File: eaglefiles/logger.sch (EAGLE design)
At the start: 15 parts, among them IC2 MAX641CSA

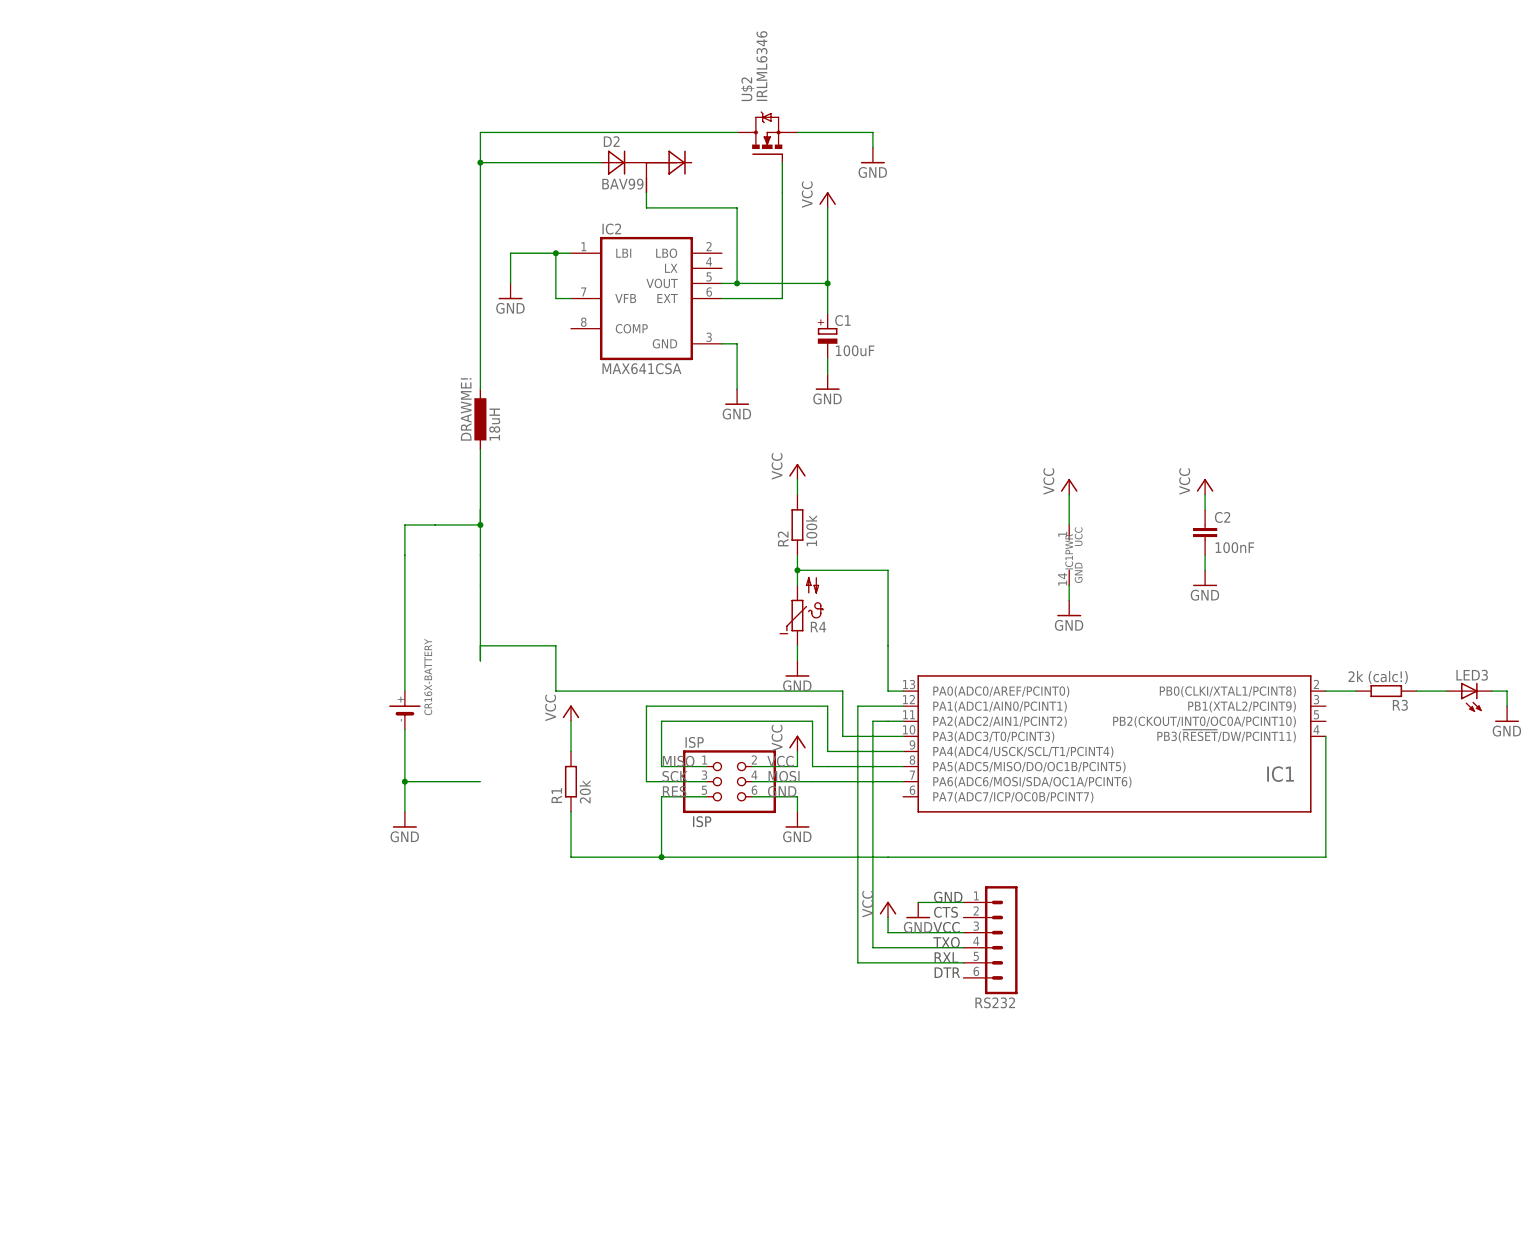
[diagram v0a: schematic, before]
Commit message: UART-USB Adapter and TSIC-506 added
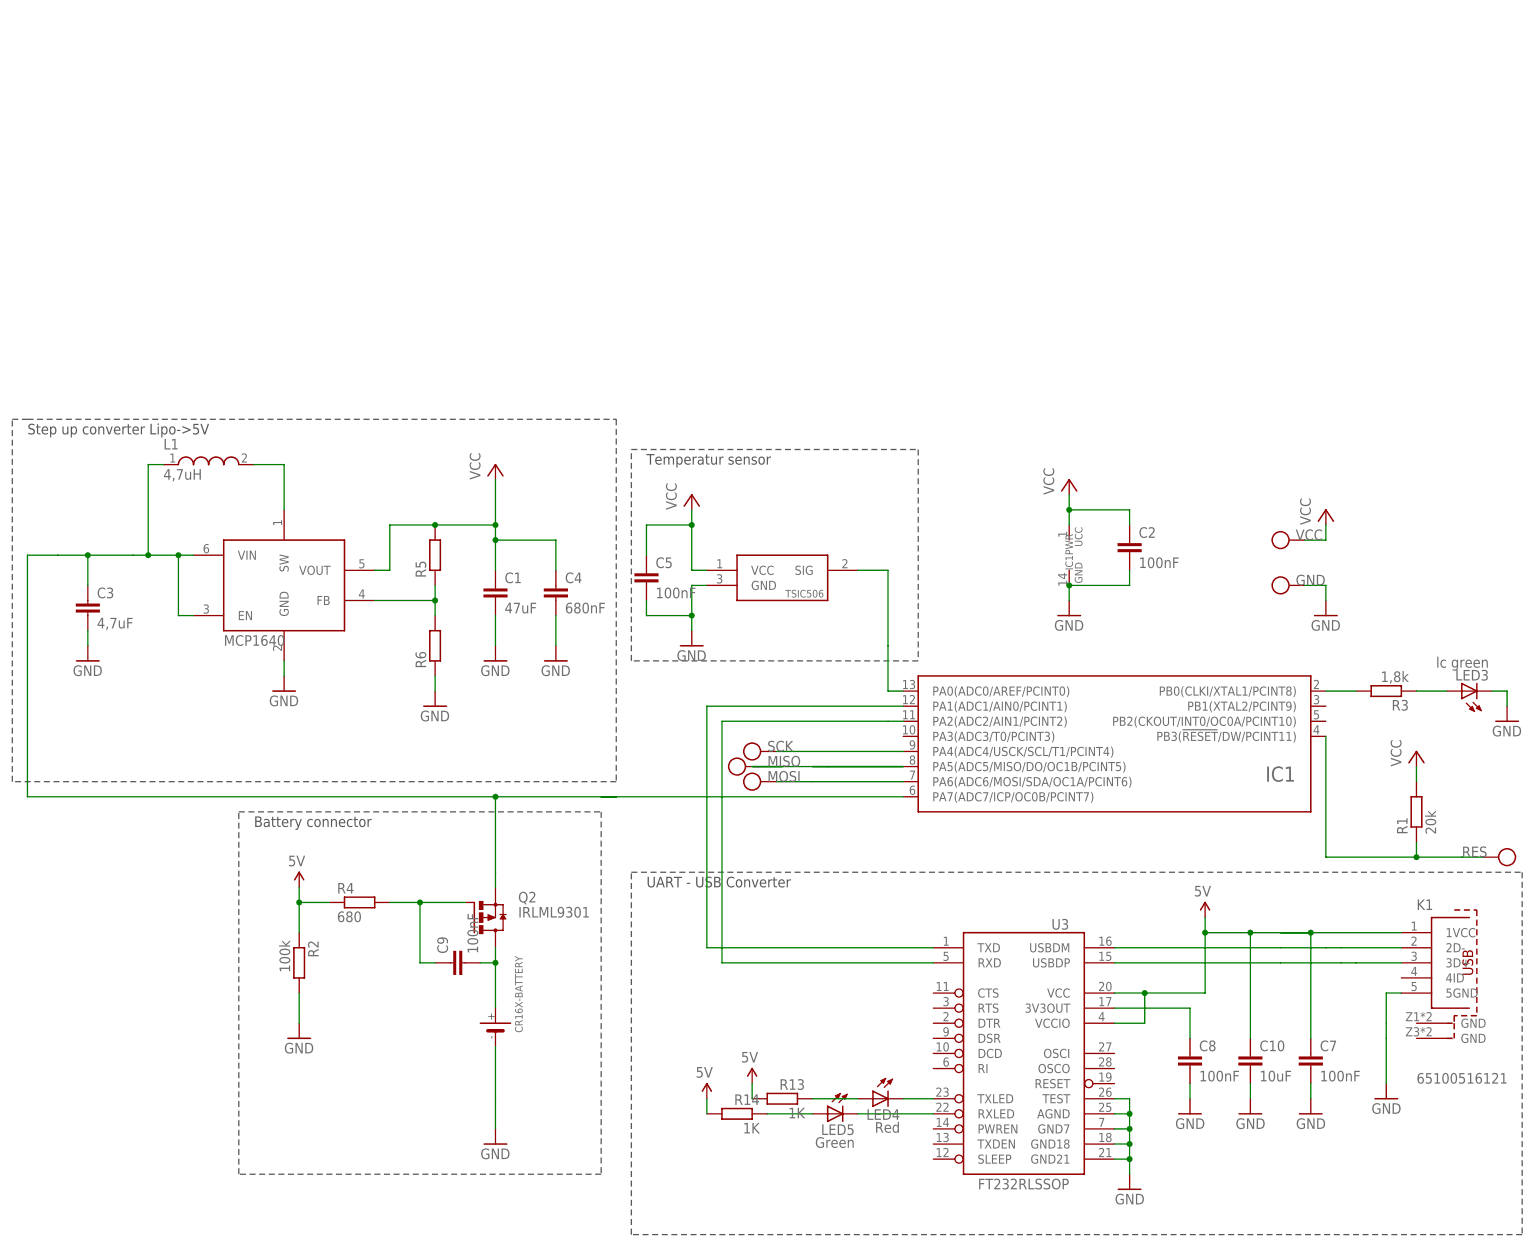
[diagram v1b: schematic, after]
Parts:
- removed D2: BAV99, 0liver:BAV99
- removed DRAWME!: 18uH, rcl:L-EUL8530M
- removed IC2: MAX641CSA, maxim:MAX641CSA
- removed ISP: (no value), pinhead:PINHD-2X3
- removed RS232: (no value), con-lstb:MA06-1
- added C10: 10uF, rcl:C-EUC1206
- added C3: 4,7uF, rcl:C-EUC1206K
- added C4: 680nF, resistor:C-EUC0805
- added C5, C8, C9: 100nF, rcl:C-EUC0603
- added C7: 100nF, rcl:C-EUC1206
- added K1: 65100516121, Input-Output_Connectors_rev15d:65100516121
- added L1: 4,7uH, EagleLibrary_Wuerth_Elektronik_eiSos_rev16a:WE-TPC_3816
- added LED4: Red, SparkFun:LED0603
- added LED5: Green, SparkFun:LED0603
- added Q2: IRLML9301, 0liver:IRLML9301
- added R13, R14: 1K, rcl:R-EU_R1206
- added R5, R6: (no value), resistor:R-EU_R1206
- added U$10, U$11, U$12, U$7, U$8, U$9: (no value), 0liver:PIN1.27
- added U1: MCP1640, karlnet-parts:MCP1640
- added U3: FT232RLSSOP, SparkFun:FT232RLSSOP
- C1: value 100uF -> 47uF; device rcl:CPOL-EU153CLV-0505 -> resistor:C-EUC1206
- LED3: value (none) -> lc green; device led:LEDSML0603 -> led:LEDCHIPLED_0603
- R2: device rcl:R-EU_R1206 -> eagle-ltspice:RR1206
- R3: value 2k (calc!) -> 1,8k
- R4: value (none) -> 680; device ptc-ntc:NTC640 -> eagle-ltspice:RR1206
- U$2: value IRLML6346 -> TSIC-506; device 0liver:IRLML6346 -> 0liver:TSIC-506
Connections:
- removed net D1: IC1IC.PA3(ADC3/T0/PCINT3), U$1.P$1
- removed net N$8: D2.A, DRAWME!.1, U$2.D
- new net 5V: R2.1, R4.1
- new net N$3: C8.1, U3.3V3OUT
- new net N$4: LED4.A, R13.1
- new net N$6: C9.2, Q2.D, U$1.P$1
- new net RXLED: LED5.C, U3.RXLED
- new net SW: L1.2, U1.SW
- new net TXLED: LED4.C, U3.TXLED
- new net USB_D+: K1.3D+, U3.USBDP
- new net USB_D-: K1.2D-, U3.USBDM
- new net VSUPPLY: C3.1, IC1IC.PA7(ADC7/ICP/OC0B/PCINT7), L1.1, Q2.S, U1.EN, U1.VIN
- new net V_USB: C10.1, C7.1, C9.1, K1.1VCC, Q2.G, R13.2, R14.2, R4.2, U3.VCC, U3.VCCIO
- net GND: now also C1.2, C10.2, C3.2, C4.2, C5.2, C7.2, C8.2, K1.5GND, R2.2, R6.1, U$10.P$1, U$2.GND, U1.GND, U3.AGND, U3.GND18, U3.GND21, U3.GND7, U3.TEST; no longer C1.-, IC2.GND, IC2.LBI, IC2.VFB, ISP.6, R4.1, RS232.1, U$2.S
- net MISO: now also U$7.P$1; no longer ISP.1
- net MOSI: now also U$11.P$1; no longer ISP.4
- net N$1: now also U3.RXD; no longer RS232.4
- net N$2: now also U$2.SIG; no longer R2.1, R4.2
- net N$32: now also U3.TXD; no longer RS232.5
- net N$5: now also R5.1, R6.2, U1.FB; no longer IC2.EXT, U$2.G
- net N$7: now also LED5.A, R14.1; no longer DRAWME!.2
- net RES: now also U$9.P$1; no longer ISP.5
- net SCK: now also U$8.P$1; no longer ISP.3
- net VCC: now also C1.1, C4.1, C5.1, R5.2, U$12.P$1, U$2.VCC, U1.VOUT; no longer C1.+, D2.M, IC2.VOUT, ISP.2, R2.2, RS232.3
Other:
- note added: "Battery connector"
- note added: "Step up converter Lipo->5V"
- note added: "Temperatur sensor"
- note added: "UART - USB Converter"
- note removed: "CTS"
- note removed: "DTR"
- note removed: "GND"
- note removed: "ISP"
- note removed: "RXL"
- note removed: "TXO"
- note removed: "VCC"
- moved on the sheet: C2, R1, R2

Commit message: Added ctr for reset
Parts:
- added C6: 100nF, rcl:C-EUC0603
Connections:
- new net N$8: C6.2, U3.DTR
- net RES: now also C6.1
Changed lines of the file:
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@@
 <part name="R4" library="eagle-ltspice" deviceset="R" device="R1206" value="680"/>
 <part name="C10" library="rcl" deviceset="C-EU" device="C1206" value="10uF"/>
+<part name="C6" library="rcl" deviceset="C-EU" device="C0603" value="100nF"/>
 </parts>
 <sheets>
@@
 <instance part="R4" gate="G$1" x="-43.18" y="-10.16"/>
 <instance part="C10" gate="G$1" x="106.68" y="-35.56"/>
+<instance part="C6" gate="G$1" x="43.18" y="-30.48" rot="R90"/>
 </instances>
 <busses>
@@
 <pinref part="R1" gate="G$1" pin="1"/>
 <pinref part="U$9" gate="G$1" pin="P$1"/>
+<pinref part="C6" gate="G$1" pin="1"/>
+<wire x1="40.64" y1="-30.48" x2="35.56" y2="-30.48" width="0.1524" layer="91"/>
+<wire x1="35.56" y1="-30.48" x2="35.56" y2="-2.54" width="0.1524" layer="91"/>
+<wire x1="35.56" y1="-2.54" x2="119.38" y2="-2.54" width="0.1524" layer="91"/>
+<junction x="119.38" y="-2.54"/>
 </segment>
 </net>
@@
 </segment>
 </net>
+<net name="N$8" class="0">
+<segment>
+<pinref part="U3" gate="G$1" pin="DTR"/>
+<pinref part="C6" gate="G$1" pin="2"/>
+<wire x1="53.34" y1="-30.48" x2="48.26" y2="-30.48" width="0.1524" layer="91"/>
+</segment>
+</net>
